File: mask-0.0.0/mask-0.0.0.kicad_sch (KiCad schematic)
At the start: 1 part, among them SW1 SW_Push

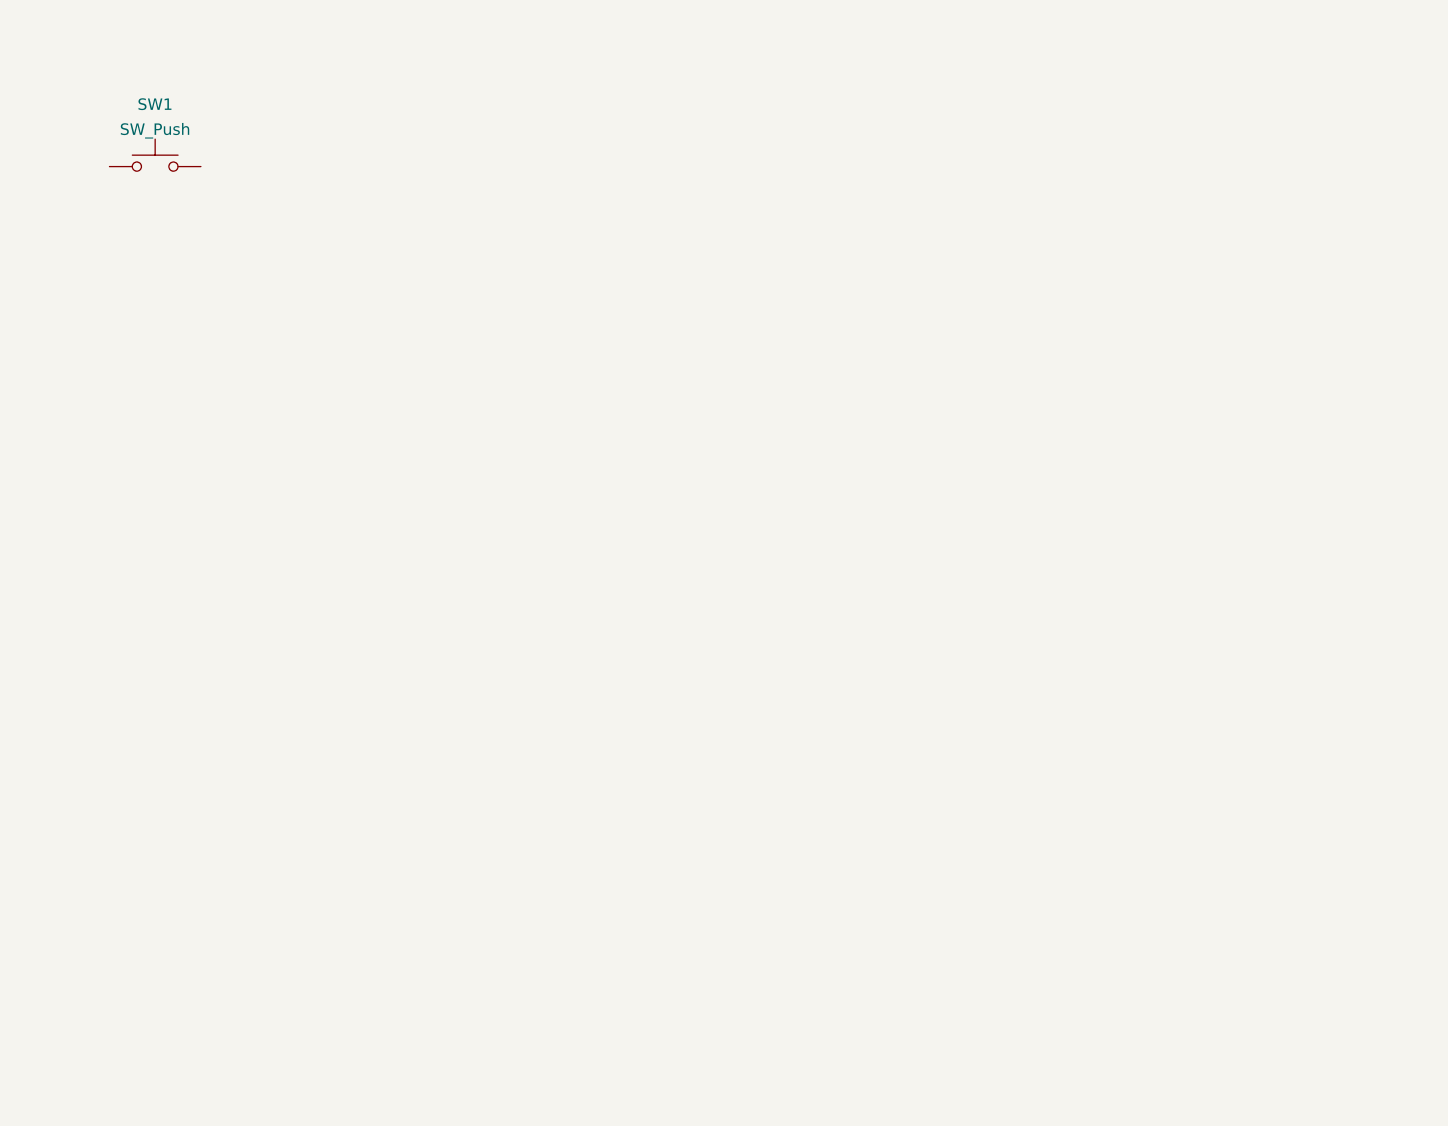
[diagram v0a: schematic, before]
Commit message: draw basic key-matrix
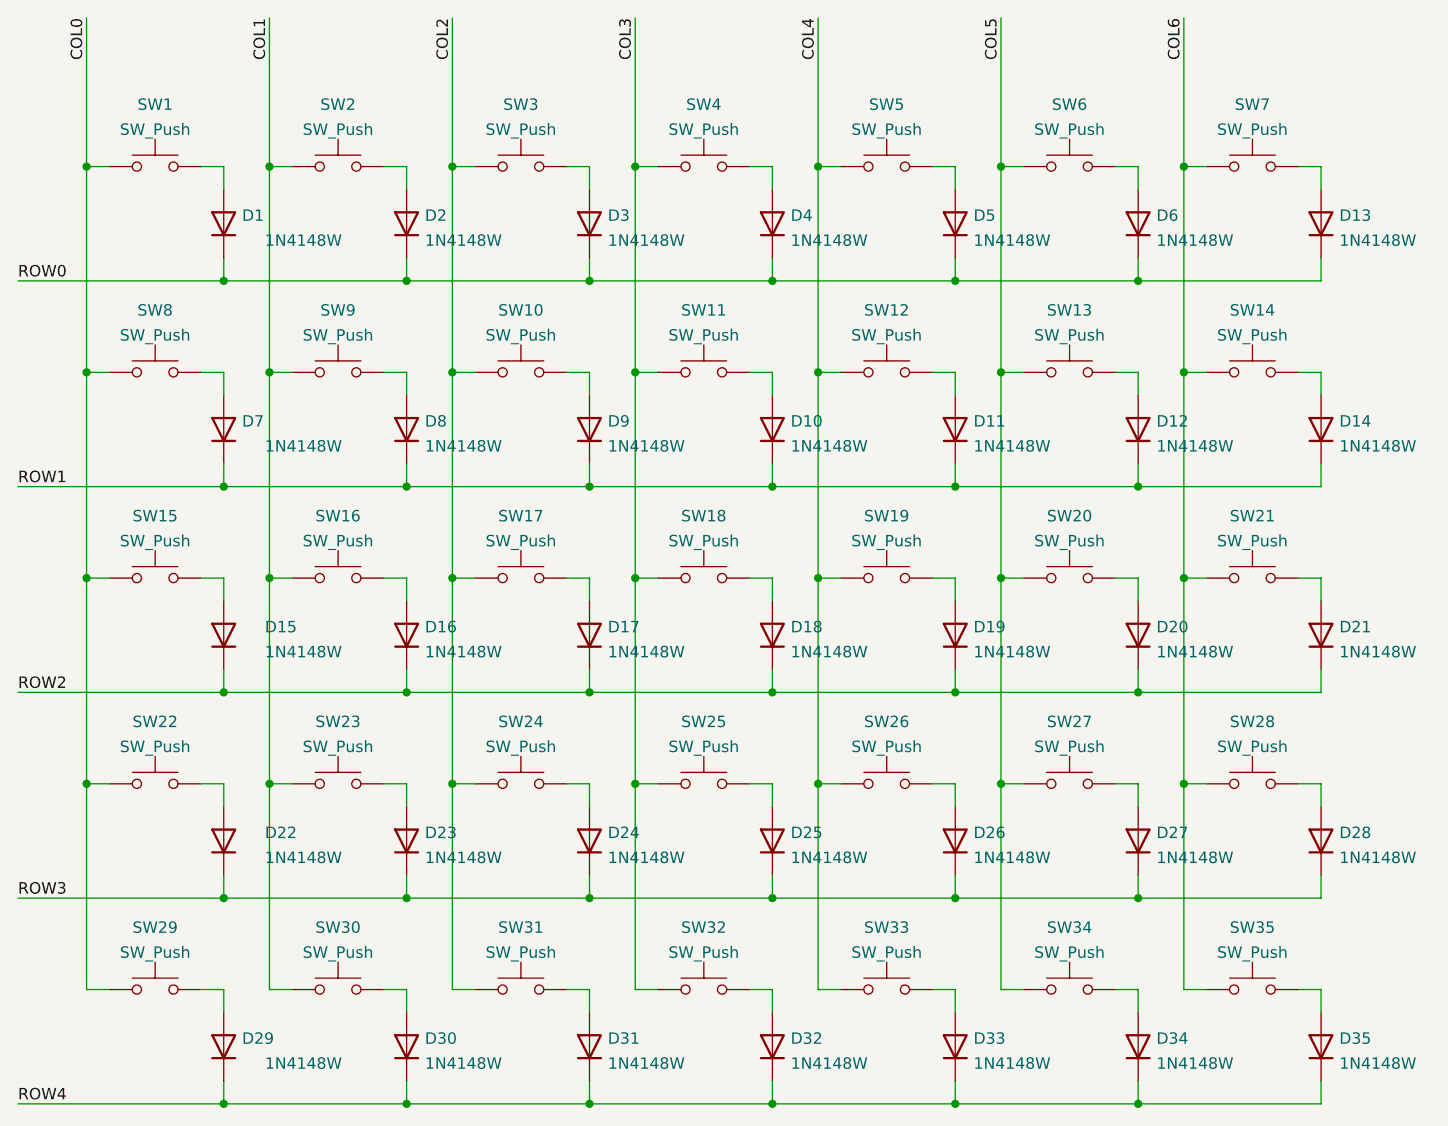
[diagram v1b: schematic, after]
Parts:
- added D1, D10, D11, D12, D13, D14, D15, D16, D17, D18, D19, D2, D20, D21, D22, D23, D24, D25, D26, D27, D28, D29, D3, D30, D31, D32, D33, D34, D35, D4, D5, D6, D7, D8, D9: 1N4148W, Diode_SMD:D_SOD-123, symbol Diode:1N4148W
- added SW10, SW11, SW12, SW13, SW14, SW15, SW16, SW17, SW18, SW19, SW2, SW20, SW21, SW22, SW23, SW24, SW25, SW26, SW27, SW28, SW29, SW3, SW30, SW31, SW32, SW33, SW34, SW35, SW4, SW5, SW6, SW7, SW8, SW9: SW_Push, Button_Switch_Keyboard_Swappable:SW_Cherry_MX_1.00u_Kailh_Socket_TopBottom, symbol Switch:SW_Push
- SW1: footprint Button_Switch_Keyboard:SW_Cherry_MX_1.00u_PCB -> Button_Switch_Keyboard_Swappable:SW_Cherry_MX_1.00u_Kailh_Socket_TopBottom
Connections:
- net COL0: now reaches SW1.1
- net COL0: now also SW15.1, SW22.1, SW29.1, SW8.1
- net at SW1.2: now also D1.2 (A)
- new net: D23.2 (A), SW23.2
- new net: D33.2 (A), SW33.2
- new net: D13.2 (A), SW7.2
- new net: D25.2 (A), SW25.2
- new net: D27.2 (A), SW27.2
- new net: D10.2 (A), SW11.2
- new net: D22.2 (A), SW22.2
- new net: D12.2 (A), SW13.2
- new net: D8.2 (A), SW9.2
- new net: D6.2 (A), SW6.2
- new net: D4.2 (A), SW4.2
- new net: D28.2 (A), SW28.2
- new net: D7.2 (A), SW8.2
- new net: D34.2 (A), SW34.2
- new net: D17.2 (A), SW17.2
- new net: D31.2 (A), SW31.2
- new net: D20.2 (A), SW20.2
- new net: D9.2 (A), SW10.2
- new net: D5.2 (A), SW5.2
- new net: D3.2 (A), SW3.2
- new net: D24.2 (A), SW24.2
- new net: D2.2 (A), SW2.2
- new net: D14.2 (A), SW14.2
- new net: D21.2 (A), SW21.2
- new net: D16.2 (A), SW16.2
- new net: D30.2 (A), SW30.2
- new net: D11.2 (A), SW12.2
- new net: D29.2 (A), SW29.2
- new net: D19.2 (A), SW19.2
- new net: D26.2 (A), SW26.2
- new net: D18.2 (A), SW18.2
- new net: D35.2 (A), SW35.2
- new net: D15.2 (A), SW15.2
- new net: D32.2 (A), SW32.2
- new net COL1: SW16.1, SW2.1, SW23.1, SW30.1, SW9.1
- new net COL2: SW10.1, SW17.1, SW24.1, SW3.1, SW31.1
- new net COL3: SW11.1, SW18.1, SW25.1, SW32.1, SW4.1
- new net COL4: SW12.1, SW19.1, SW26.1, SW33.1, SW5.1
- new net COL5: SW13.1, SW20.1, SW27.1, SW34.1, SW6.1
- new net COL6: SW14.1, SW21.1, SW28.1, SW35.1, SW7.1
- new net ROW0: D1.1 (K), D13.1 (K), D2.1 (K), D3.1 (K), D4.1 (K), D5.1 (K), D6.1 (K)
- new net ROW1: D10.1 (K), D11.1 (K), D12.1 (K), D14.1 (K), D7.1 (K), D8.1 (K), D9.1 (K)
- new net ROW2: D15.1 (K), D16.1 (K), D17.1 (K), D18.1 (K), D19.1 (K), D20.1 (K), D21.1 (K)
- new net ROW3: D22.1 (K), D23.1 (K), D24.1 (K), D25.1 (K), D26.1 (K), D27.1 (K), D28.1 (K)
- new net ROW4: D29.1 (K), D30.1 (K), D31.1 (K), D32.1 (K), D33.1 (K), D34.1 (K), D35.1 (K)

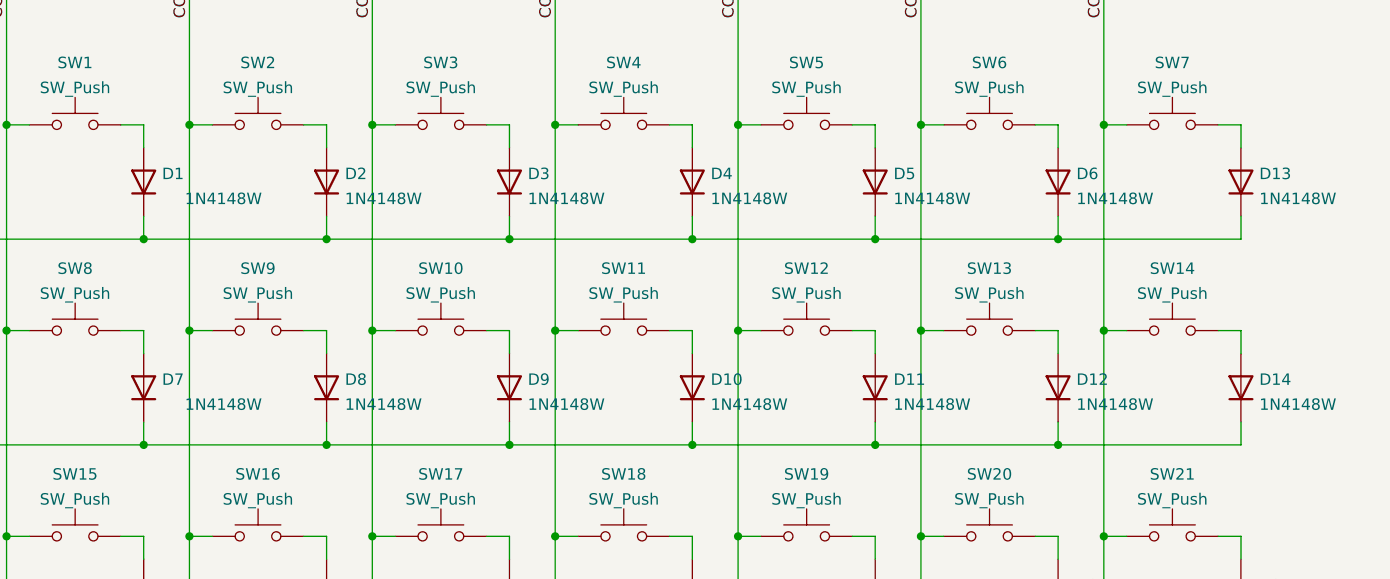
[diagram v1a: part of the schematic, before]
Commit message: change diodes package, start test positioning in correct distance
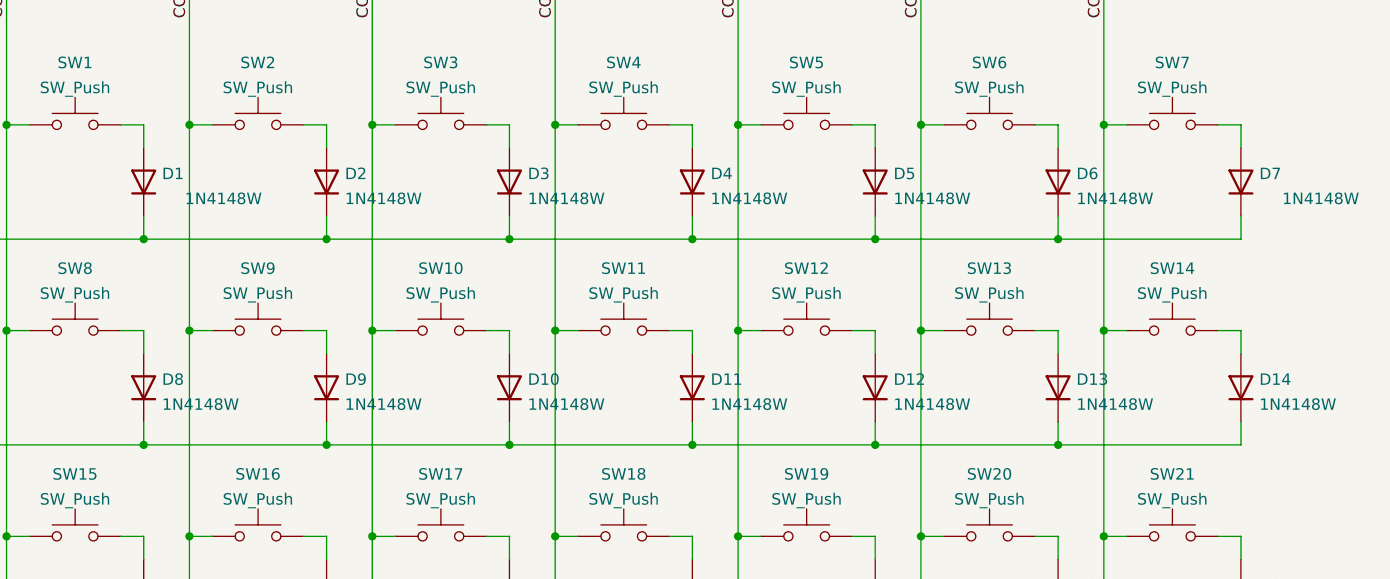
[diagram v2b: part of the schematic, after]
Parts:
- D1, D10, D11, D12, D13, D14, D15, D16, D17, D18, D19, D2, D20, D21, D22, D23, D24, D25, D26, D27, D28, D29, D3, D30, D31, D32, D33, D34, D35, D4, D5, D6, D7, D8, D9: footprint Diode_SMD:D_SOD-123 -> Diode_SMD_TopBottom:D_SOD-123_TopBottom
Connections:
- net ROW0: now also D7.1 (K); no longer D13.1 (K)
- net ROW1: now also D13.1 (K); no longer D7.1 (K)
- net at SW7.2: now also D7.2 (A); no longer D13.2 (A)
- net at SW11.2: now also D11.2 (A); no longer D10.2 (A)
- net at SW13.2: now also D13.2 (A); no longer D12.2 (A)
- net at D8.2 (A): now also SW8.2; no longer SW9.2
- net at SW10.2: now also D10.2 (A); no longer D9.2 (A)
- net at SW12.2: now also D12.2 (A); no longer D11.2 (A)
- new net: D9.2 (A), SW9.2
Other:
- moved on the sheet: D10, D11, D12, D13, D7, D8, D9

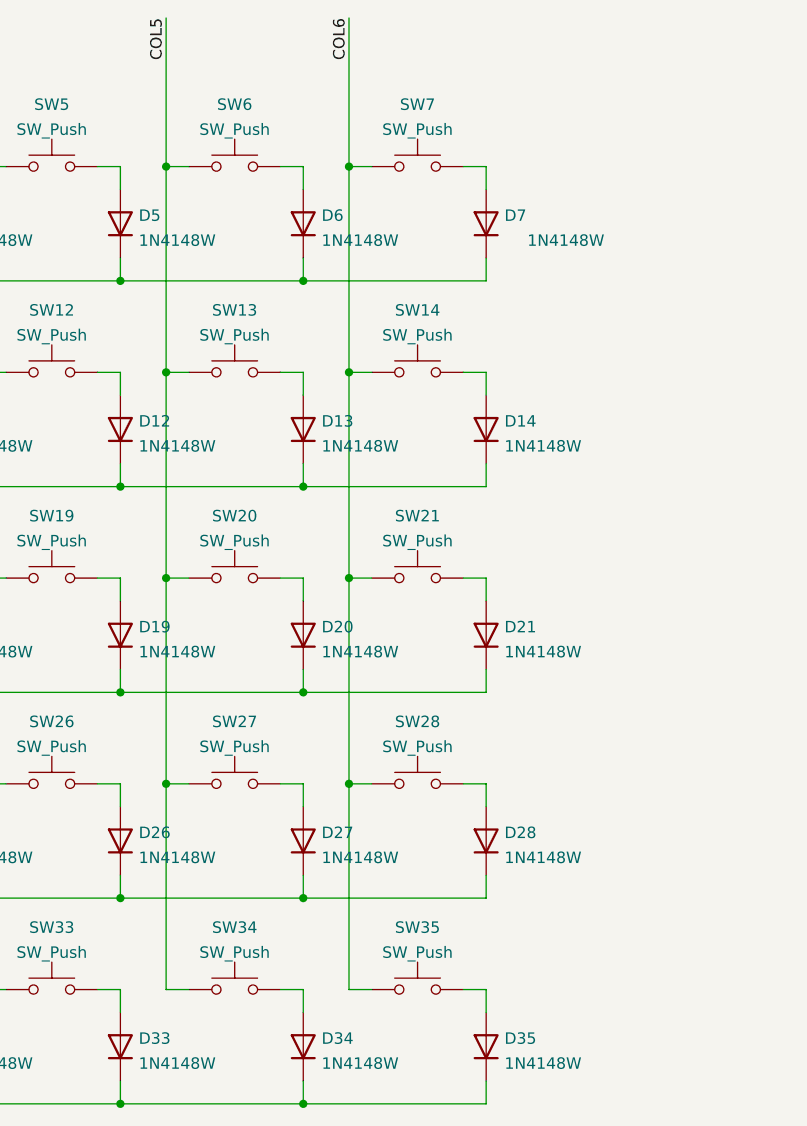
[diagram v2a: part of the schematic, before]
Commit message: test-place buttons (only ortholinear, not shifted)
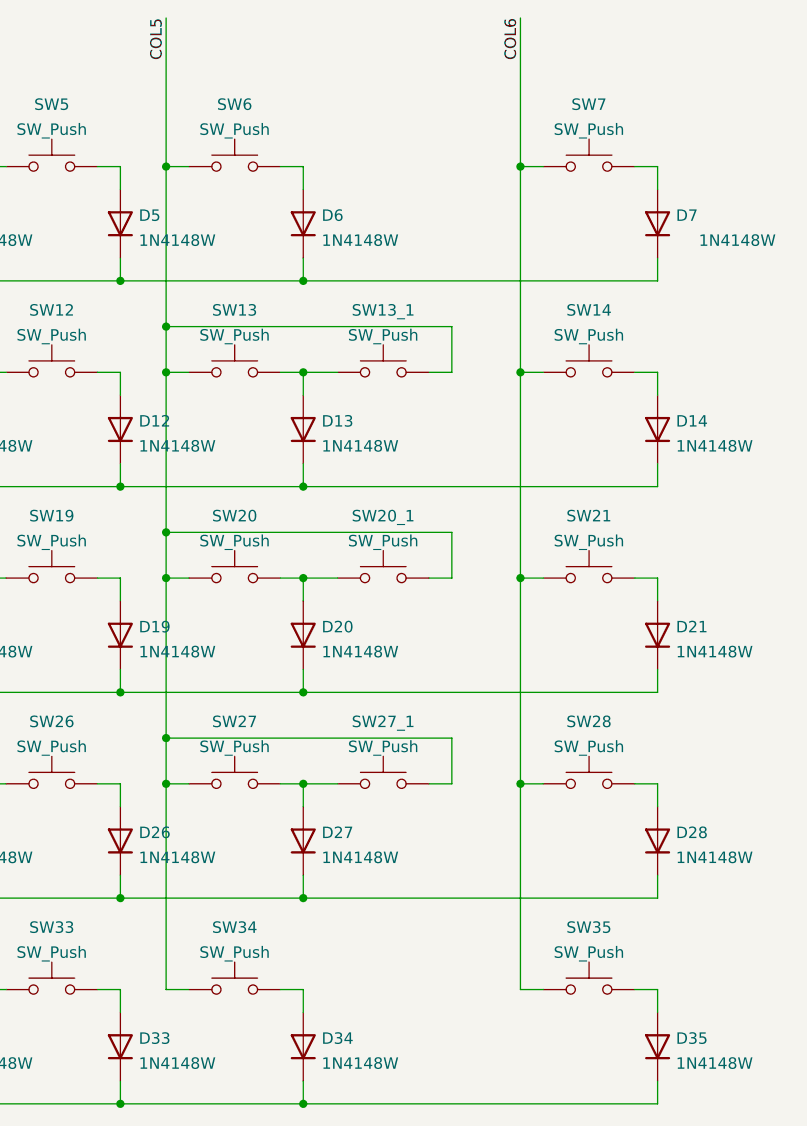
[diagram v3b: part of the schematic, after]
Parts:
- added SW13_1, SW20_1, SW27_1: SW_Push, Button_Switch_Keyboard_Swappable:SW_Cherry_MX_2.00u_Kailh_Socket_NoStabilizer_TopBottom, symbol Switch:SW_Push
- SW31, SW32, SW33, SW34, SW35: footprint Button_Switch_Keyboard_Swappable:SW_Cherry_MX_1.00u_Kailh_Socket_TopBottom -> Button_Switch_Keyboard_Swappable:SW_Cherry_MX_1.50u_Kailh_Socket_TopBottom
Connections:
- net COL5: now also SW13_1.2, SW20_1.2, SW27_1.2
- net at D27.2 (A), SW27.2: now also SW27_1.1
- net at D13.2 (A), SW13.2: now also SW13_1.1
- net at D20.2 (A), SW20.2: now also SW20_1.1
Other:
- moved on the sheet: D14, D21, D28, D35, D7, SW14, SW21, SW28, SW35, SW7

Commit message: first test layout
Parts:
- SW31: footprint Button_Switch_Keyboard_Swappable:SW_Cherry_MX_1.50u_Kailh_Socket_TopBottom -> Button_Switch_Keyboard_Swappable:SW_Cherry_MX_1.25u_Kailh_Socket_TopBottom
- SW32, SW33, SW34, SW35: footprint Button_Switch_Keyboard_Swappable:SW_Cherry_MX_1.50u_Kailh_Socket_TopBottom -> Button_Switch_Keyboard_Swappable:SW_Cherry_MX_1.00u_Kailh_Socket_TopBottom
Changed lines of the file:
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@@
     (property "Reference" "SW31" (id 0) (at 127 125.1924 0))
     (property "Value" "SW_Push" (id 1) (at 127 127.9675 0))
-    (property "Footprint" "Button_Switch_Keyboard_Swappable:SW_Cherry_MX_1.50u_Kailh_Socket_TopBottom" (id 2) (at 127 127 0)
+    (property "Footprint" "Button_Switch_Keyboard_Swappable:SW_Cherry_MX_1.25u_Kailh_Socket_TopBottom" (id 2) (at 127 127 0)
       (effects (font (size 1.27 1.27)) hide)
     )
@@
     (property "Reference" "SW32" (id 0) (at 147.32 125.1924 0))
     (property "Value" "SW_Push" (id 1) (at 147.32 127.9675 0))
-    (property "Footprint" "Button_Switch_Keyboard_Swappable:SW_Cherry_MX_1.50u_Kailh_Socket_TopBottom" (id 2) (at 147.32 127 0)
+    (property "Footprint" "Button_Switch_Keyboard_Swappable:SW_Cherry_MX_1.00u_Kailh_Socket_TopBottom" (id 2) (at 147.32 127 0)
       (effects (font (size 1.27 1.27)) hide)
     )
@@
     (property "Reference" "SW33" (id 0) (at 167.64 125.1924 0))
     (property "Value" "SW_Push" (id 1) (at 167.64 127.9675 0))
-    (property "Footprint" "Button_Switch_Keyboard_Swappable:SW_Cherry_MX_1.50u_Kailh_Socket_TopBottom" (id 2) (at 167.64 127 0)
+    (property "Footprint" "Button_Switch_Keyboard_Swappable:SW_Cherry_MX_1.00u_Kailh_Socket_TopBottom" (id 2) (at 167.64 127 0)
       (effects (font (size 1.27 1.27)) hide)
     )
@@
     (property "Reference" "SW34" (id 0) (at 187.96 125.1924 0))
     (property "Value" "SW_Push" (id 1) (at 187.96 127.9675 0))
-    (property "Footprint" "Button_Switch_Keyboard_Swappable:SW_Cherry_MX_1.50u_Kailh_Socket_TopBottom" (id 2) (at 187.96 127 0)
+    (property "Footprint" "Button_Switch_Keyboard_Swappable:SW_Cherry_MX_1.00u_Kailh_Socket_TopBottom" (id 2) (at 187.96 127 0)
       (effects (font (size 1.27 1.27)) hide)
     )
@@
     (property "Reference" "SW35" (id 0) (at 227.33 125.1924 0))
     (property "Value" "SW_Push" (id 1) (at 227.33 127.9675 0))
-    (property "Footprint" "Button_Switch_Keyboard_Swappable:SW_Cherry_MX_1.50u_Kailh_Socket_TopBottom" (id 2) (at 227.33 127 0)
+    (property "Footprint" "Button_Switch_Keyboard_Swappable:SW_Cherry_MX_1.00u_Kailh_Socket_TopBottom" (id 2) (at 227.33 127 0)
       (effects (font (size 1.27 1.27)) hide)
     )
@@
     )
     (path "/2ebc2251-9777-416a-994b-055771e9c60b"
-      (reference "SW31") (unit 1) (value "SW_Push") (footprint "Button_Switch_Keyboard_Swappable:SW_Cherry_MX_1.50u_Kailh_Socket_TopBottom")
+      (reference "SW31") (unit 1) (value "SW_Push") (footprint "Button_Switch_Keyboard_Swappable:SW_Cherry_MX_1.25u_Kailh_Socket_TopBottom")
     )
     (path "/e5443503-168a-4e3e-a918-6e6f179a3a8d"
-      (reference "SW32") (unit 1) (value "SW_Push") (footprint "Button_Switch_Keyboard_Swappable:SW_Cherry_MX_1.50u_Kailh_Socket_TopBottom")
+      (reference "SW32") (unit 1) (value "SW_Push") (footprint "Button_Switch_Keyboard_Swappable:SW_Cherry_MX_1.00u_Kailh_Socket_TopBottom")
     )
     (path "/0acb42a0-acc4-405e-8d77-912524bec326"
-      (reference "SW33") (unit 1) (value "SW_Push") (footprint "Button_Switch_Keyboard_Swappable:SW_Cherry_MX_1.50u_Kailh_Socket_TopBottom")
+      (reference "SW33") (unit 1) (value "SW_Push") (footprint "Button_Switch_Keyboard_Swappable:SW_Cherry_MX_1.00u_Kailh_Socket_TopBottom")
     )
     (path "/4e2af24f-c73b-4dac-b2e5-112606b1e77e"
-      (reference "SW34") (unit 1) (value "SW_Push") (footprint "Button_Switch_Keyboard_Swappable:SW_Cherry_MX_1.50u_Kailh_Socket_TopBottom")
+      (reference "SW34") (unit 1) (value "SW_Push") (footprint "Button_Switch_Keyboard_Swappable:SW_Cherry_MX_1.00u_Kailh_Socket_TopBottom")
     )
     (path "/a00fe42a-f38f-4c77-865f-eb9b291c6af6"
-      (reference "SW35") (unit 1) (value "SW_Push") (footprint "Button_Switch_Keyboard_Swappable:SW_Cherry_MX_1.50u_Kailh_Socket_TopBottom")
-    )
-  )
+      (reference "SW35") (unit 1) (value "SW_Push") (footprint "Button_Switch_Keyboard_Swappable:SW_Cherry_MX_1.00u_Kailh_Socket_TopBottom")
+    )
+  )
